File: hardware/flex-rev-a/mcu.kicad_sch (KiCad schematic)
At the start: 1 part, among them U1 ISP2454-LX

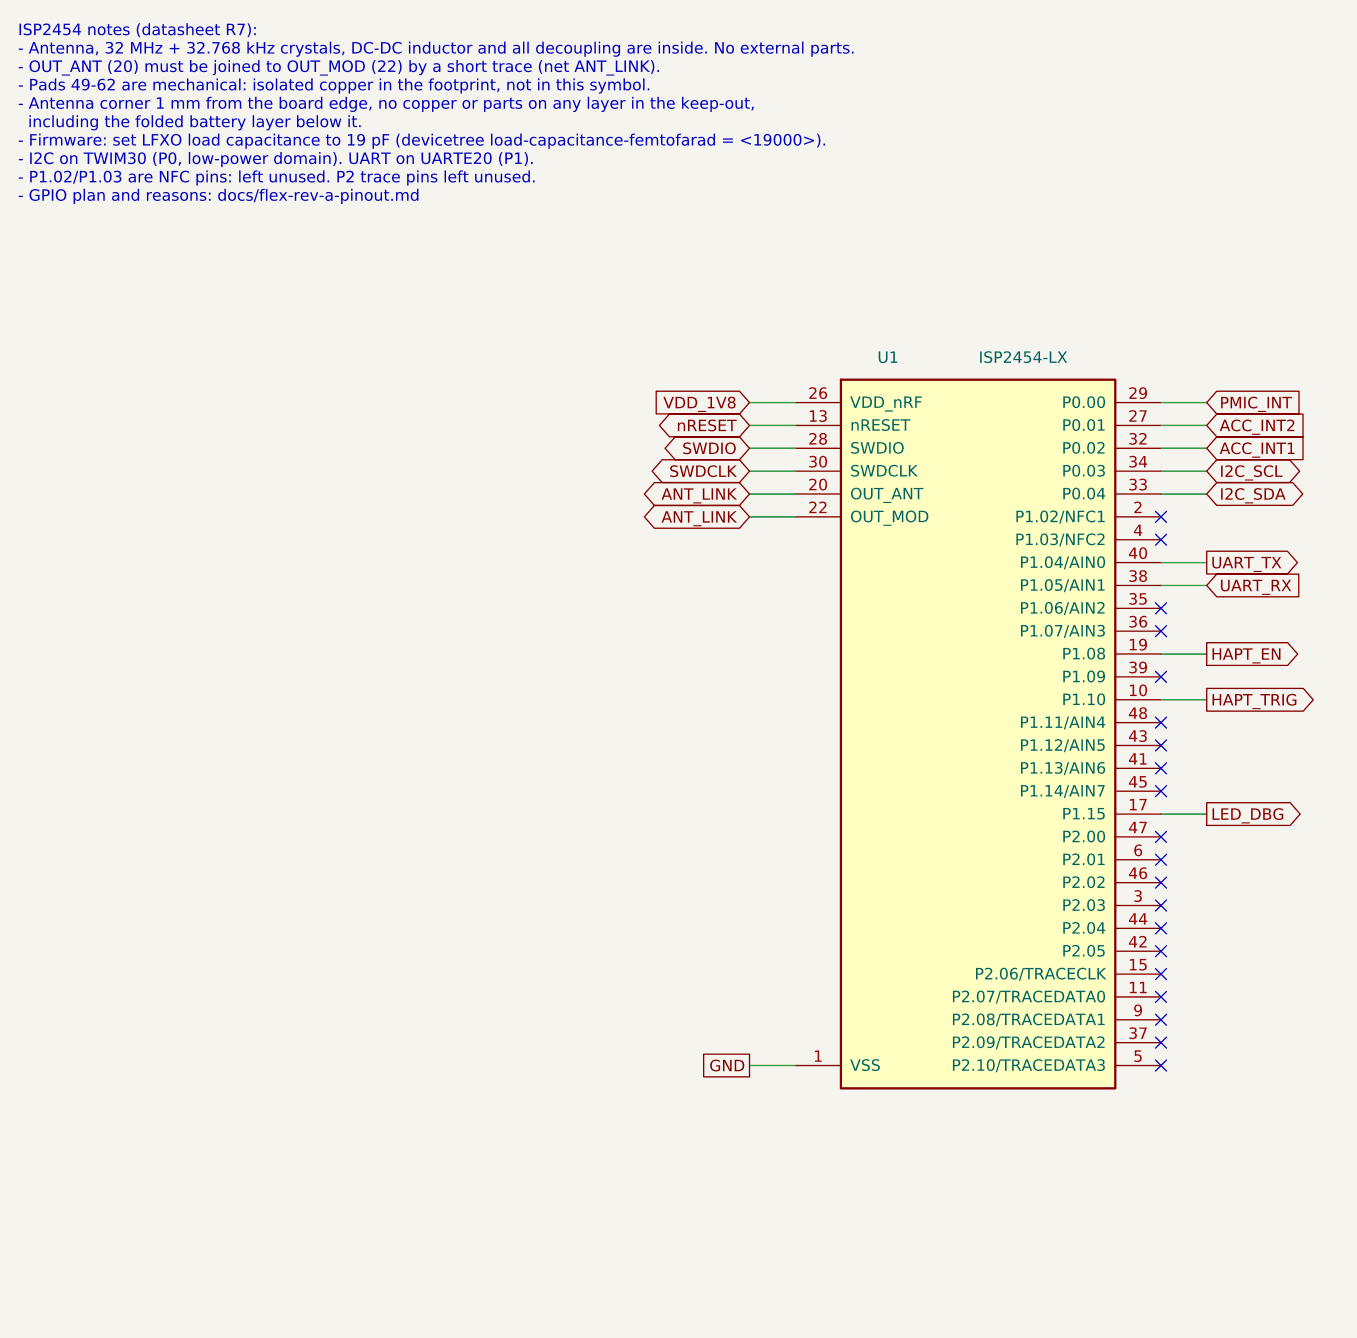
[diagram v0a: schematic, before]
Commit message: Add ISP2454 footprint and move all signals to outer-row pads
Footprint built from datasheet section 4.1 (R7), with an antenna
keep-out rule area per section 4.3. GPIO plan changed so every signal
uses an outer-row pad and the flex needs no via-in-pad.

Co-Authored-By: Claude Opus 5.5 <noreply@anthropic.com>
Claude-Session: https://claude.ai/code/session_01Q9Z9S4cetxefbuzxgfQdaw
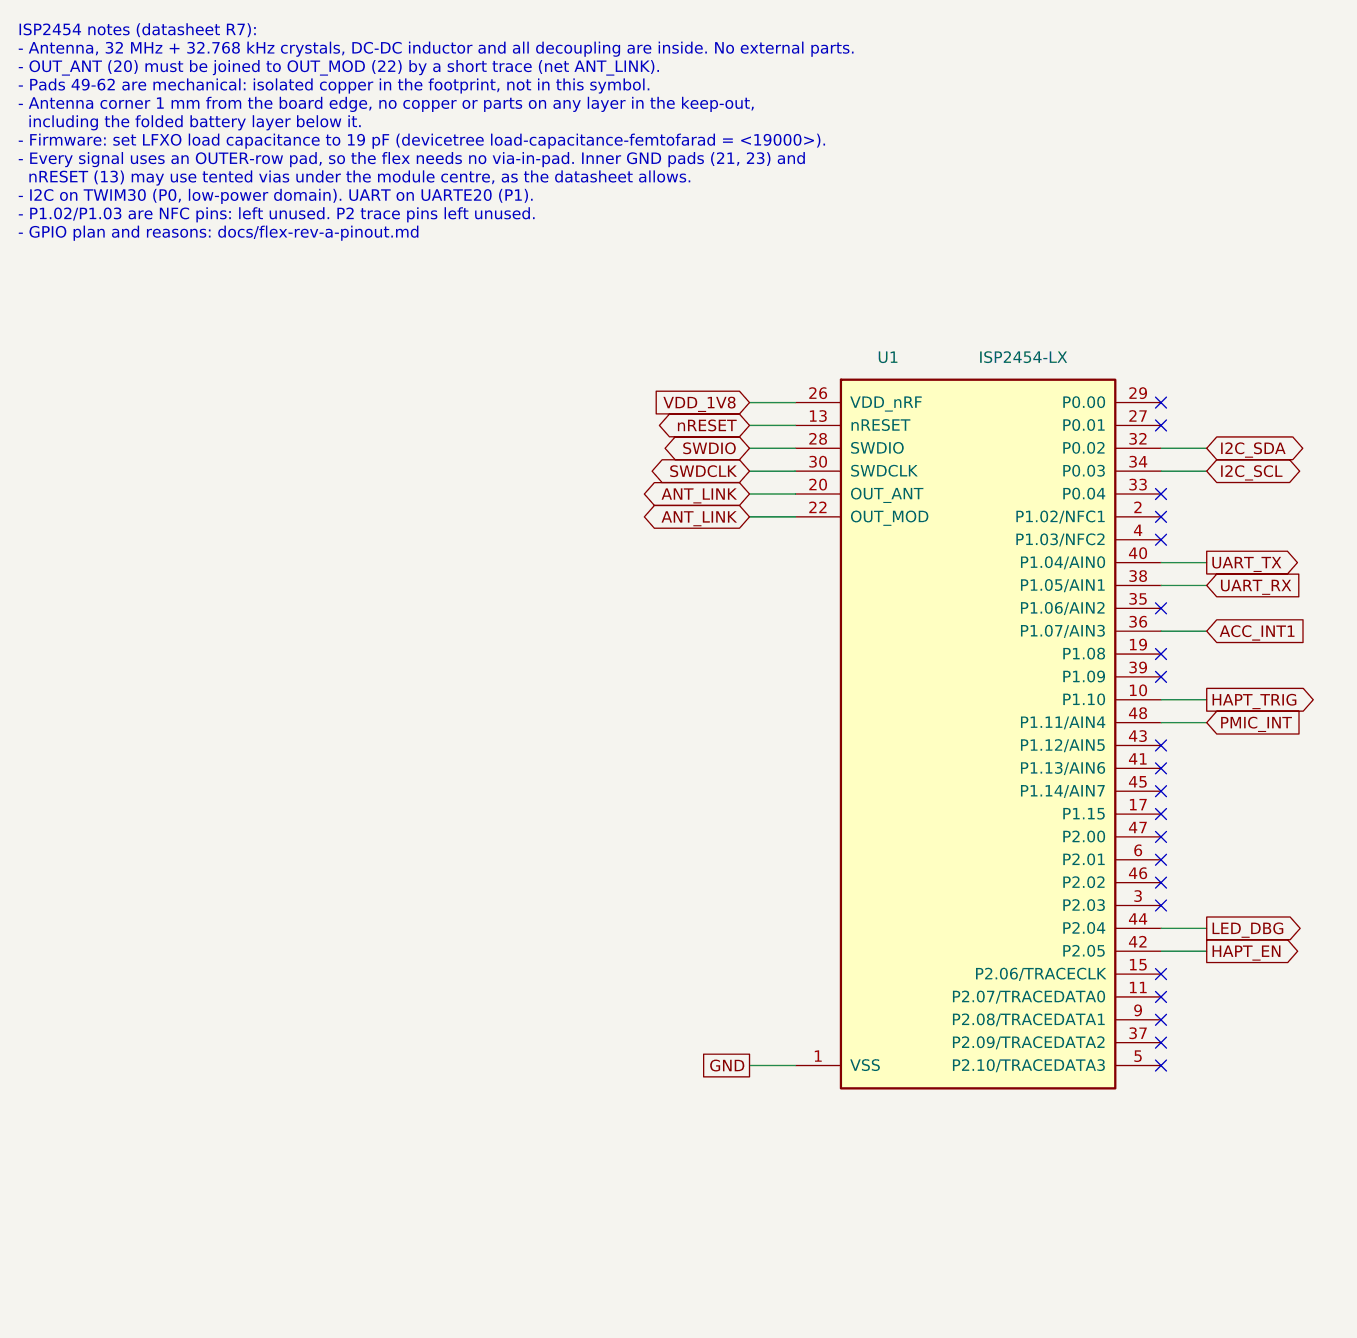
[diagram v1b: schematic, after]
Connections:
- net ACC_INT1: now also U1.36 (P1.07/AIN3); no longer U1.32 (P0.02)
- net HAPT_EN: now also U1.42 (P2.05); no longer U1.19 (P1.08)
- net I2C_SDA: now also U1.32 (P0.02); no longer U1.33 (P0.04)
- net LED_DBG: now also U1.44 (P2.04); no longer U1.17 (P1.15)
- net PMIC_INT: now also U1.48 (P1.11/AIN4); no longer U1.29 (P0.00)
- net ACC_INT2: no longer names the net of U1.27 (P0.01)
- no-connect marks 20 -> 21
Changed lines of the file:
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@@
   (global_label "ANT_LINK" (shape bidirectional) (at 101.6 74.93 180) (fields_autoplaced) (effects (font (size 1.27 1.27)) (justify right))
     (property "Intersheetrefs" "${INTERSHEET_REFS}" (at 0 0 0) (effects (font (size 1.27 1.27)) hide)))
-  (wire (pts (xy 147.32 62.23) (xy 152.4 62.23)) (stroke (width 0) (type default)))
-  (global_label "PMIC_INT" (shape input) (at 152.4 62.23 0) (fields_autoplaced) (effects (font (size 1.27 1.27)) (justify left))
-    (property "Intersheetrefs" "${INTERSHEET_REFS}" (at 0 0 0) (effects (font (size 1.27 1.27)) hide)))
-  (wire (pts (xy 147.32 64.77) (xy 152.4 64.77)) (stroke (width 0) (type default)))
-  (global_label "ACC_INT2" (shape input) (at 152.4 64.77 0) (fields_autoplaced) (effects (font (size 1.27 1.27)) (justify left))
-    (property "Intersheetrefs" "${INTERSHEET_REFS}" (at 0 0 0) (effects (font (size 1.27 1.27)) hide)))
+  (no_connect (at 147.32 62.23))
+  (no_connect (at 147.32 64.77))
   (wire (pts (xy 147.32 67.31) (xy 152.4 67.31)) (stroke (width 0) (type default)))
-  (global_label "ACC_INT1" (shape input) (at 152.4 67.31 0) (fields_autoplaced) (effects (font (size 1.27 1.27)) (justify left))
+  (global_label "I2C_SDA" (shape bidirectional) (at 152.4 67.31 0) (fields_autoplaced) (effects (font (size 1.27 1.27)) (justify left))
     (property "Intersheetrefs" "${INTERSHEET_REFS}" (at 0 0 0) (effects (font (size 1.27 1.27)) hide)))
   (wire (pts (xy 147.32 69.85) (xy 152.4 69.85)) (stroke (width 0) (type default)))
   (global_label "I2C_SCL" (shape bidirectional) (at 152.4 69.85 0) (fields_autoplaced) (effects (font (size 1.27 1.27)) (justify left))
     (property "Intersheetrefs" "${INTERSHEET_REFS}" (at 0 0 0) (effects (font (size 1.27 1.27)) hide)))
-  (wire (pts (xy 147.32 72.39) (xy 152.4 72.39)) (stroke (width 0) (type default)))
-  (global_label "I2C_SDA" (shape bidirectional) (at 152.4 72.39 0) (fields_autoplaced) (effects (font (size 1.27 1.27)) (justify left))
-    (property "Intersheetrefs" "${INTERSHEET_REFS}" (at 0 0 0) (effects (font (size 1.27 1.27)) hide)))
+  (no_connect (at 147.32 72.39))
   (no_connect (at 147.32 74.93))
   (no_connect (at 147.32 77.47))
@@
     (property "Intersheetrefs" "${INTERSHEET_REFS}" (at 0 0 0) (effects (font (size 1.27 1.27)) hide)))
   (no_connect (at 147.32 85.09))
-  (no_connect (at 147.32 87.63))
-  (wire (pts (xy 147.32 90.17) (xy 152.4 90.17)) (stroke (width 0) (type default)))
-  (global_label "HAPT_EN" (shape output) (at 152.4 90.17 0) (fields_autoplaced) (effects (font (size 1.27 1.27)) (justify left))
+  (wire (pts (xy 147.32 87.63) (xy 152.4 87.63)) (stroke (width 0) (type default)))
+  (global_label "ACC_INT1" (shape input) (at 152.4 87.63 0) (fields_autoplaced) (effects (font (size 1.27 1.27)) (justify left))
     (property "Intersheetrefs" "${INTERSHEET_REFS}" (at 0 0 0) (effects (font (size 1.27 1.27)) hide)))
+  (no_connect (at 147.32 90.17))
   (no_connect (at 147.32 92.71))
   (wire (pts (xy 147.32 95.25) (xy 152.4 95.25)) (stroke (width 0) (type default)))
   (global_label "HAPT_TRIG" (shape output) (at 152.4 95.25 0) (fields_autoplaced) (effects (font (size 1.27 1.27)) (justify left))
     (property "Intersheetrefs" "${INTERSHEET_REFS}" (at 0 0 0) (effects (font (size 1.27 1.27)) hide)))
-  (no_connect (at 147.32 97.79))
+  (wire (pts (xy 147.32 97.79) (xy 152.4 97.79)) (stroke (width 0) (type default)))
+  (global_label "PMIC_INT" (shape input) (at 152.4 97.79 0) (fields_autoplaced) (effects (font (size 1.27 1.27)) (justify left))
+    (property "Intersheetrefs" "${INTERSHEET_REFS}" (at 0 0 0) (effects (font (size 1.27 1.27)) hide)))
   (no_connect (at 147.32 100.33))
   (no_connect (at 147.32 102.87))
   (no_connect (at 147.32 105.41))
-  (wire (pts (xy 147.32 107.95) (xy 152.4 107.95)) (stroke (width 0) (type default)))
-  (global_label "LED_DBG" (shape output) (at 152.4 107.95 0) (fields_autoplaced) (effects (font (size 1.27 1.27)) (justify left))
-    (property "Intersheetrefs" "${INTERSHEET_REFS}" (at 0 0 0) (effects (font (size 1.27 1.27)) hide)))
+  (no_connect (at 147.32 107.95))
   (no_connect (at 147.32 110.49))
   (no_connect (at 147.32 113.03))
   (no_connect (at 147.32 115.57))
   (no_connect (at 147.32 118.11))
-  (no_connect (at 147.32 120.65))
-  (no_connect (at 147.32 123.19))
+  (wire (pts (xy 147.32 120.65) (xy 152.4 120.65)) (stroke (width 0) (type default)))
+  (global_label "LED_DBG" (shape output) (at 152.4 120.65 0) (fields_autoplaced) (effects (font (size 1.27 1.27)) (justify left))
+    (property "Intersheetrefs" "${INTERSHEET_REFS}" (at 0 0 0) (effects (font (size 1.27 1.27)) hide)))
+  (wire (pts (xy 147.32 123.19) (xy 152.4 123.19)) (stroke (width 0) (type default)))
+  (global_label "HAPT_EN" (shape output) (at 152.4 123.19 0) (fields_autoplaced) (effects (font (size 1.27 1.27)) (justify left))
+    (property "Intersheetrefs" "${INTERSHEET_REFS}" (at 0 0 0) (effects (font (size 1.27 1.27)) hide)))
   (no_connect (at 147.32 125.73))
   (no_connect (at 147.32 128.27))
@@
     (pin "25")
     (pin "31")
-    (instances (project "flex-rev-a" (path "/17f1ffbf-f672-4ef8-9802-24862f78423c/c80ac41d-356f-4de9-b75d-a908c60d2f6b" (reference "U1") (unit 1))))
+    (instances (project "flex-rev-a" (path "/f1a047c3-8922-464f-af19-ac9fc5db330b/17001d3b-fbd8-4f96-b500-59fa238486df" (reference "U1") (unit 1))))
   )
-  (text "ISP2454 notes (datasheet R7):\n- Antenna, 32 MHz + 32.768 kHz crystals, DC-DC inductor and all decoupling are inside. No external parts.\n- OUT_ANT (20) must be joined to OUT_MOD (22) by a short trace (net ANT_LINK).\n- Pads 49-62 are mechanical: isolated copper in the footprint, not in this symbol.\n- Antenna corner 1 mm from the board edge, no copper or parts on any layer in the keep-out,\n  including the folded battery layer below it.\n- Firmware: set LFXO load capacitance to 19 pF (devicetree load-capacitance-femtofarad = <19000>).\n- I2C on TWIM30 (P0, low-power domain). UART on UARTE20 (P1).\n- P1.02/P1.03 are NFC pins: left unused. P2 trace pins left unused.\n- GPIO plan and reasons: docs/flex-rev-a-pinout.md" (at 20.32 20.32 0) (effects (font (size 1.27 1.27)) (justify left top)))
+  (text "ISP2454 notes (datasheet R7):\n- Antenna, 32 MHz + 32.768 kHz crystals, DC-DC inductor and all decoupling are inside. No external parts.\n- OUT_ANT (20) must be joined to OUT_MOD (22) by a short trace (net ANT_LINK).\n- Pads 49-62 are mechanical: isolated copper in the footprint, not in this symbol.\n- Antenna corner 1 mm from the board edge, no copper or parts on any layer in the keep-out,\n  including the folded battery layer below it.\n- Firmware: set LFXO load capacitance to 19 pF (devicetree load-capacitance-femtofarad = <19000>).\n- Every signal uses an OUTER-row pad, so the flex needs no via-in-pad. Inner GND pads (21, 23) and\n  nRESET (13) may use tented vias under the module centre, as the datasheet allows.\n- I2C on TWIM30 (P0, low-power domain). UART on UARTE20 (P1).\n- P1.02/P1.03 are NFC pins: left unused. P2 trace pins left unused.\n- GPIO plan and reasons: docs/flex-rev-a-pinout.md" (at 20.32 20.32 0) (effects (font (size 1.27 1.27)) (justify left top)))
 )

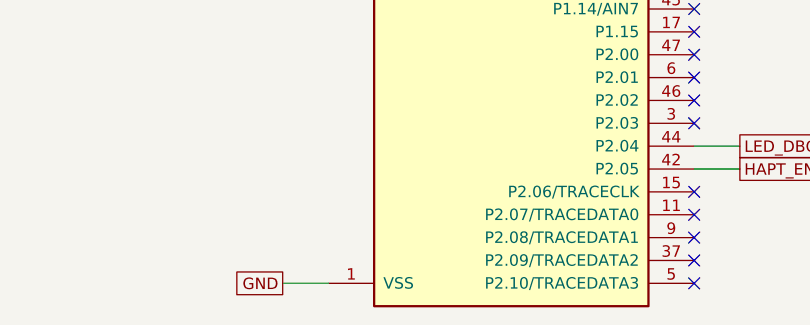
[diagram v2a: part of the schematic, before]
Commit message: Finish rev A schematic pass: clean ERC, BOM with LCSC numbers
- ERC 0 errors, 0 warnings: the ISP2454 symbol's ground pins renamed from
  VSS to GND (same pins), so they no longer clash with the GND label.
- Sensors: larger LIS2DW12 symbol so pin names and GND symbols no longer
  overlap. Dock: connector mirrored and TVS spacing widened for
  readability. No connectivity changes.
- bom.csv: JLCPCB-style columns with LCSC numbers checked on lcsc.com;
  ISP2454-LX and nPM1304-QEAA have none. Pads, jumper and net tie excluded.
- All 50 references annotated and unique; PDF replotted; README status
  table, ERC notes and plan progress updated.

Co-Authored-By: Claude Opus 5.5 <noreply@anthropic.com>
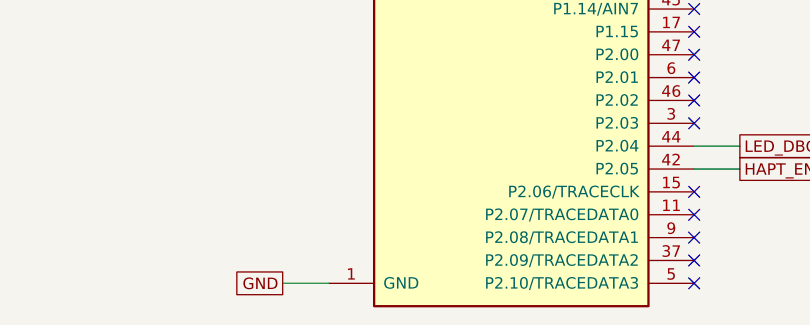
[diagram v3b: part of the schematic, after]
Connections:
- net VSS renamed GND
